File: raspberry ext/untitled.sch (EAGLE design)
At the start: 12 parts, among them IC1 MAX485ST3485

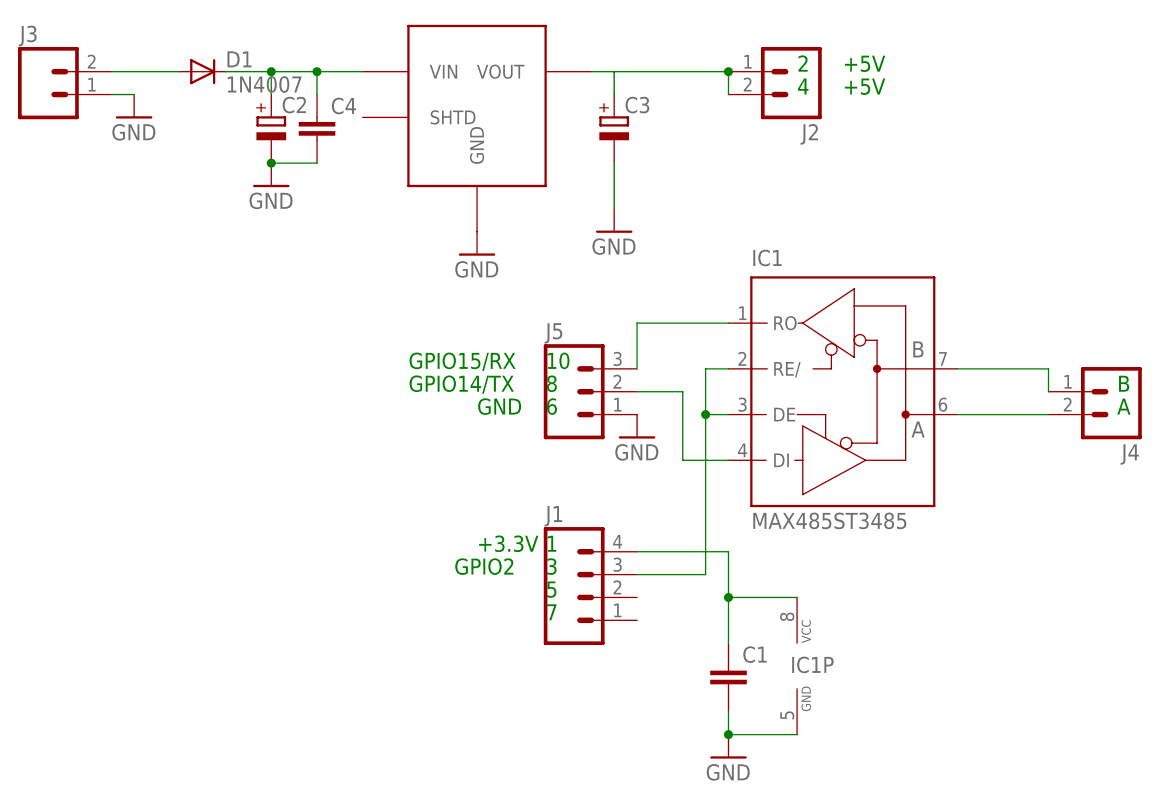
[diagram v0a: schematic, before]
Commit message: - Done wirewrap of raspberry extension!
git-svn-id: svn://mule/net/hardware/trunk@664 1a6b750e-079f-425f-90e7-3a118970be6b
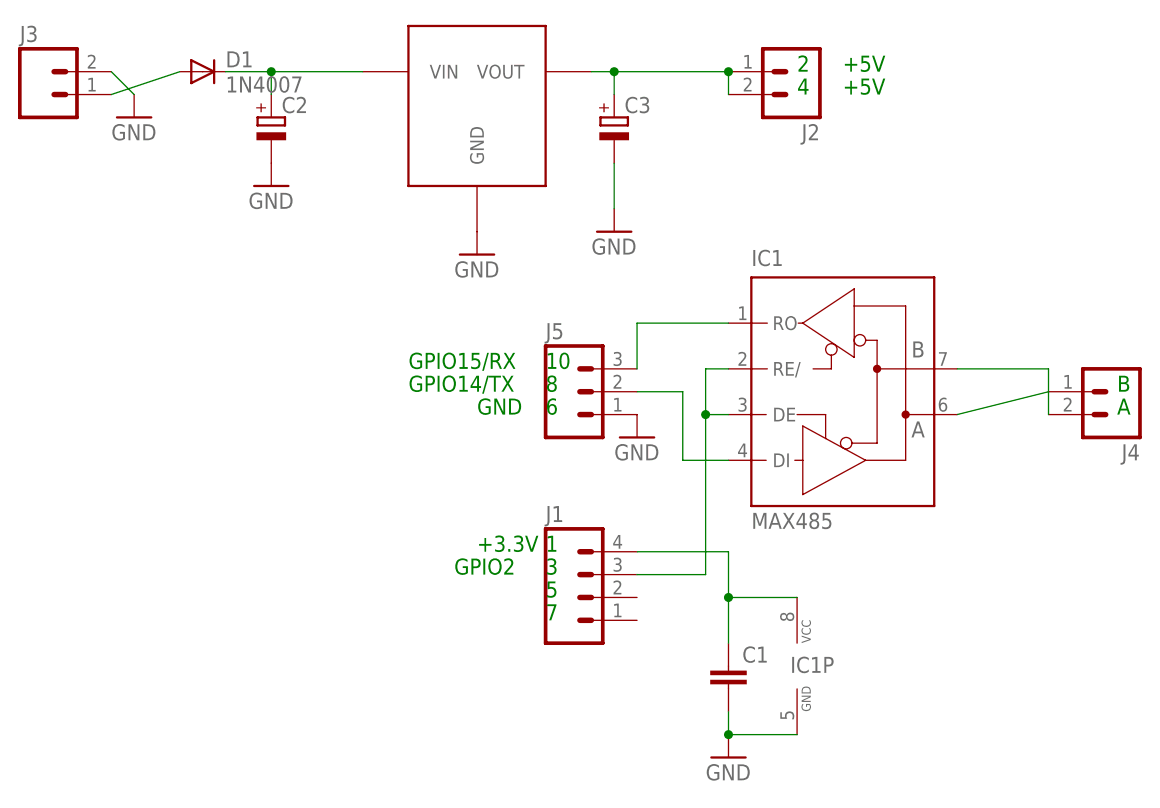
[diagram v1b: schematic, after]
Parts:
- removed C4: (no value), custom:C-EU050-025X075
- C2, C3: device custom:CPOL-EUSMD4X5.3 -> custom:CPOL-EUE2-4
- IC1: value MAX485ST3485 -> MAX485; device custom:MAX485ST3485 -> custom:MAX485
- U$1: value POLOLU-2098 -> DSUN-MP1584; device custom:POLOLU-2098 -> custom:DSUN-MP1584
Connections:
- net N$10 renamed EN
- net N$4 renamed 5V
- net N$6 renamed TX
- net N$7 renamed RX
- net N$8 renamed 3.3V
- removed net N$3: IC1G$1.A, J4.2
- removed net N$5: IC1G$1.B, J4.1
- new net A: IC1G$1.A, J4.1
- new net B: IC1G$1.B, J4.2
- net GND: now also J3.2; no longer C4.2, J3.1
- net N$1: now also J3.1; no longer J3.2
- net N$2: no longer C4.1
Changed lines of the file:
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@@
 </classes>
 <parts>
-<part name="IC1" library="custom" deviceset="MAX485" device="ST3485"/>
+<part name="IC1" library="custom" deviceset="MAX485" device="" value="MAX485"/>
 <part name="D1" library="custom" deviceset="1N4007" device=""/>
 <part name="J3" library="custom" deviceset="M02-SCREW-3.5MM" device="3.5MM"/>
 <part name="J4" library="custom" deviceset="M02-SCREW-3.5MM" device="3.5MM"/>
 <part name="GND1" library="custom" deviceset="GND" device=""/>
-<part name="U$1" library="custom" deviceset="POLOLU-2098" device=""/>
+<part name="U$1" library="custom" deviceset="DSUN-MP1584" device=""/>
 <part name="J1" library="custom" deviceset="M04" device=""/>
 <part name="J2" library="custom" deviceset="M02" device=""/>
 <part name="J5" library="custom" deviceset="M03" device=""/>
 <part name="C1" library="custom" deviceset="C-EU" device="050-025X075"/>
-<part name="C2" library="custom" deviceset="CPOL-EU" device="SMD4X5.3"/>
-<part name="C3" library="custom" deviceset="CPOL-EU" device="SMD4X5.3"/>
+<part name="C2" library="custom" deviceset="CPOL-EU" device="E2-4"/>
+<part name="C3" library="custom" deviceset="CPOL-EU" device="E2-4"/>
 <part name="GND2" library="custom" deviceset="GND" device=""/>
 <part name="GND3" library="custom" deviceset="GND" device=""/>
@@
 <part name="GND5" library="custom" deviceset="GND" device=""/>
 <part name="GND6" library="custom" deviceset="GND" device=""/>
-<part name="C4" library="custom" deviceset="C-EU" device="050-025X075"/>
 </parts>
 <sheets>
@@
 <instance part="J4" gate="G$1" x="73.66" y="35.56" rot="R180"/>
 <instance part="GND1" gate="1" x="-20.32" y="58.42"/>
-<instance part="U$1" gate="G$1" x="12.7" y="58.42"/>
+<instance part="U$1" gate="G$1" x="2.54" y="66.04"/>
 <instance part="J1" gate="G$1" x="12.7" y="15.24"/>
 <instance part="J2" gate="G$1" x="38.1" y="71.12" smashed="yes" rot="R180">
@@
 <instance part="GND5" gate="1" x="20.32" y="30.48"/>
 <instance part="GND6" gate="1" x="30.48" y="-5.08"/>
-<instance part="C4" gate="G$1" x="-15.24" y="66.04"/>
 </instances>
 <busses>
@@
 <segment>
 <pinref part="D1" gate="1" pin="A"/>
-<pinref part="J3" gate="G$1" pin="2"/>
-<wire x1="-38.1" y1="71.12" x2="-30.48" y2="71.12" width="0.1524" layer="91"/>
+<pinref part="J3" gate="G$1" pin="1"/>
+<wire x1="-38.1" y1="68.58" x2="-30.48" y2="71.12" width="0.1524" layer="91"/>
 </segment>
 </net>
@@
 <pinref part="U$1" gate="G$1" pin="VIN"/>
 <wire x1="-20.32" y1="68.58" x2="-20.32" y2="71.12" width="0.1524" layer="91"/>
-<wire x1="-20.32" y1="71.12" x2="-15.24" y2="71.12" width="0.1524" layer="91"/>
 <junction x="-20.32" y="71.12"/>
-<pinref part="C4" gate="G$1" pin="1"/>
-<wire x1="-15.24" y1="71.12" x2="-10.16" y2="71.12" width="0.1524" layer="91"/>
-<wire x1="-15.24" y1="68.58" x2="-15.24" y2="71.12" width="0.1524" layer="91"/>
-<junction x="-15.24" y="71.12"/>
+<wire x1="-20.32" y1="71.12" x2="-10.16" y2="71.12" width="0.1524" layer="91"/>
 </segment>
 </net>
@@
 <pinref part="C2" gate="G$1" pin="-"/>
 <pinref part="GND1" gate="1" pin="GND"/>
-<pinref part="C4" gate="G$1" pin="2"/>
-<wire x1="-20.32" y1="60.96" x2="-15.24" y2="60.96" width="0.1524" layer="91"/>
-<junction x="-20.32" y="60.96"/>
 </segment>
 <segment>
-<pinref part="J3" gate="G$1" pin="1"/>
+<pinref part="J3" gate="G$1" pin="2"/>
 <pinref part="GND2" gate="1" pin="GND"/>
-<wire x1="-35.56" y1="68.58" x2="-38.1" y2="68.58" width="0.1524" layer="91"/>
+<wire x1="-35.56" y1="68.58" x2="-38.1" y2="71.12" width="0.1524" layer="91"/>
 </segment>
 <segment>
@@
 </segment>
 </net>
-<net name="N$4" class="0">
+<net name="5V" class="0">
 <segment>
 <pinref part="U$1" gate="G$1" pin="VOUT"/>
@@
 <wire x1="30.48" y1="71.12" x2="30.48" y2="68.58" width="0.1524" layer="91"/>
 <junction x="30.48" y="71.12"/>
+<junction x="17.78" y="71.12"/>
 </segment>
 </net>
-<net name="N$3" class="0">
+<net name="A" class="0">
 <segment>
 <pinref part="IC1" gate="G$1" pin="A"/>
-<pinref part="J4" gate="G$1" pin="2"/>
-<wire x1="55.88" y1="33.02" x2="66.04" y2="33.02" width="0.1524" layer="91"/>
+<pinref part="J4" gate="G$1" pin="1"/>
+<wire x1="55.88" y1="33.02" x2="66.04" y2="35.56" width="0.1524" layer="91"/>
 </segment>
 </net>
-<net name="N$5" class="0">
+<net name="B" class="0">
 <segment>
-<pinref part="J4" gate="G$1" pin="1"/>
+<pinref part="J4" gate="G$1" pin="2"/>
 <pinref part="IC1" gate="G$1" pin="B"/>
-<wire x1="66.04" y1="35.56" x2="66.04" y2="38.1" width="0.1524" layer="91"/>
+<wire x1="66.04" y1="33.02" x2="66.04" y2="38.1" width="0.1524" layer="91"/>
 <wire x1="66.04" y1="38.1" x2="55.88" y2="38.1" width="0.1524" layer="91"/>
 </segment>
 </net>
-<net name="N$6" class="0">
+<net name="TX" class="0">
 <segment>
 <pinref part="J5" gate="G$1" pin="2"/>
@@
 </segment>
 </net>
-<net name="N$7" class="0">
+<net name="RX" class="0">
 <segment>
 <pinref part="J5" gate="G$1" pin="3"/>
@@
 </segment>
 </net>
-<net name="N$8" class="0">
+<net name="3.3V" class="0">
 <segment>
 <pinref part="IC1" gate="P" pin="VCC"/>
@@
 </segment>
 </net>
-<net name="N$10" class="0">
+<net name="EN" class="0">
 <segment>
 <pinref part="IC1" gate="G$1" pin="RE/"/>
